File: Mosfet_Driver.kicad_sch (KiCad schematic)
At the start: 6 parts

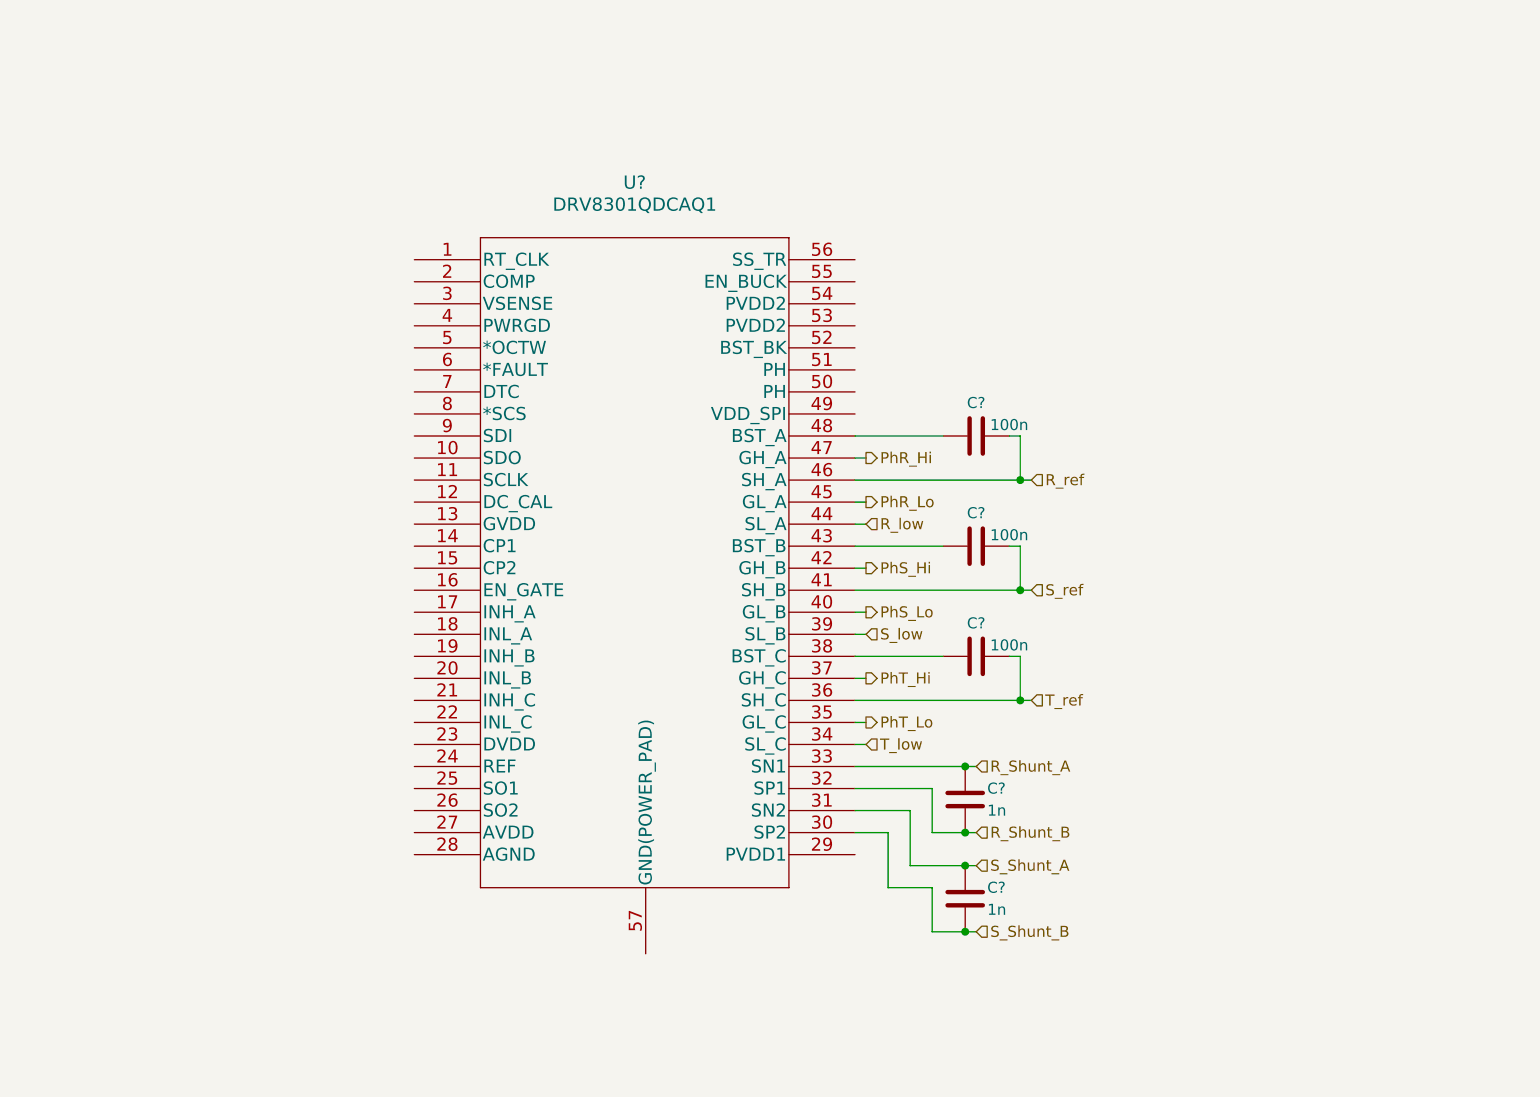
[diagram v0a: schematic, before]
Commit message: Finished basic schematic.
Need to add inline opamps and footprints to all components.
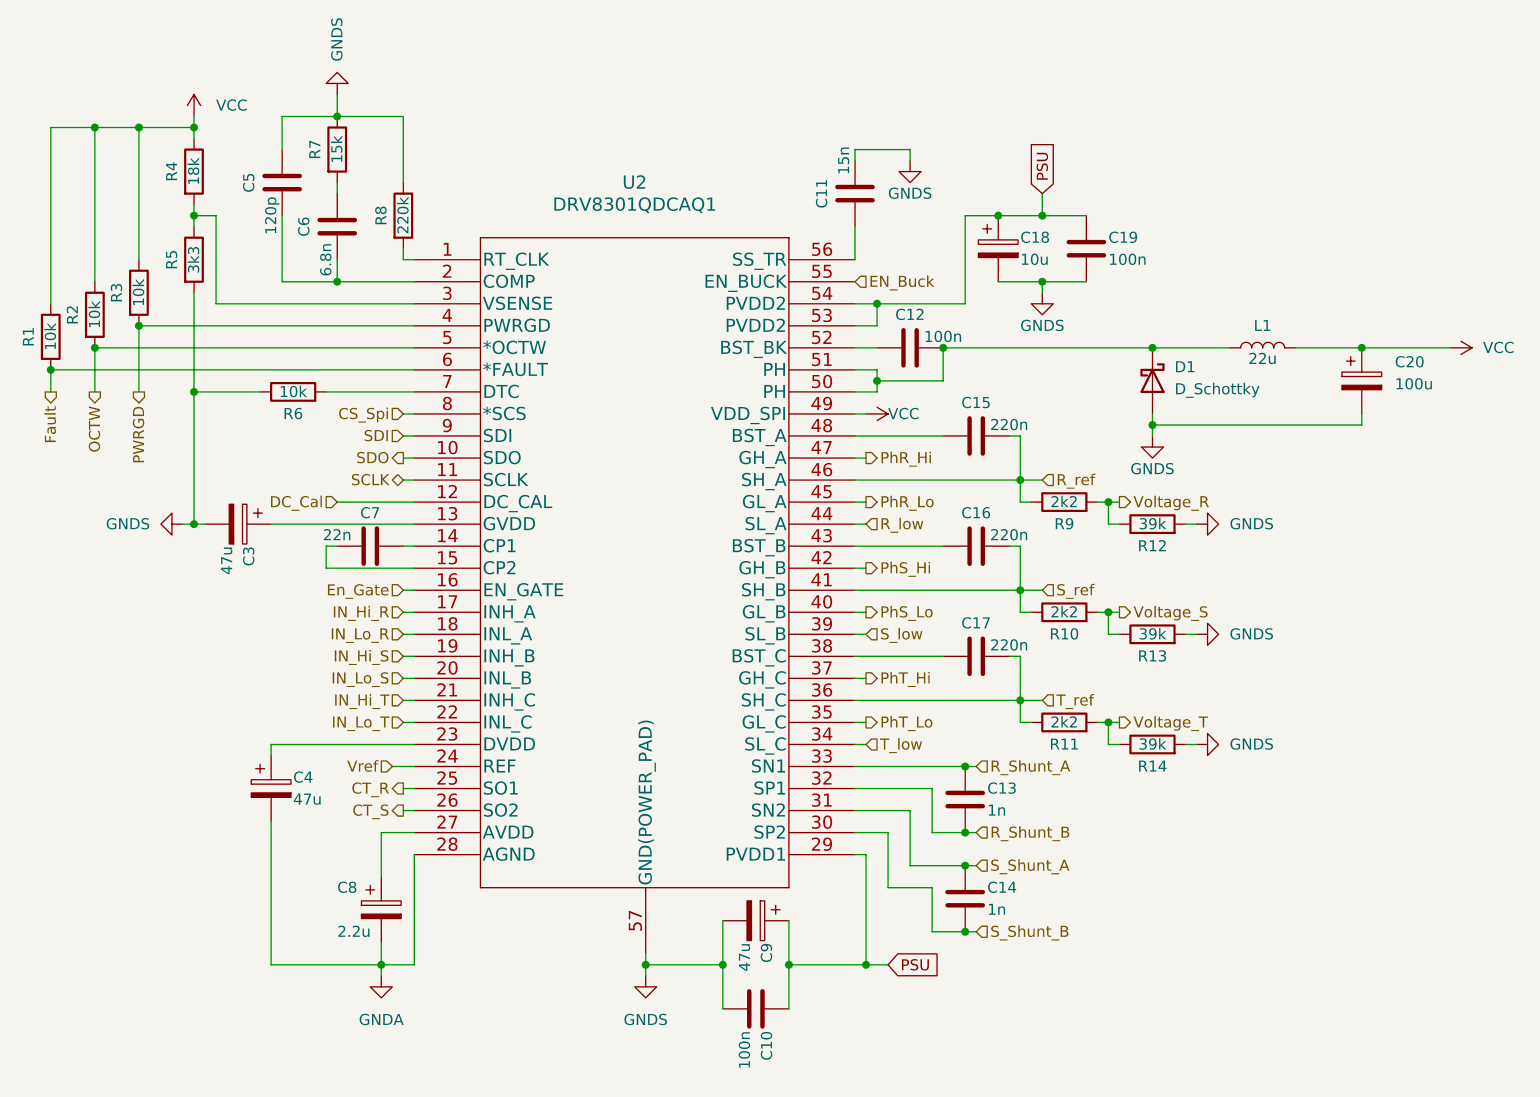
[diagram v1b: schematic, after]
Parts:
- added C10, C12, C19: 100n, symbol Device:C
- added C11: 15n, symbol Device:C
- added C18: 10u, symbol Device:C_Polarized
- added C20: 100u, symbol Device:C_Polarized
- added C3, C4, C9: 47u, symbol Device:C_Polarized
- added C5: 120p, symbol Device:C
- added C6: 6.8n, symbol Device:C
- added C7: 22n, symbol Device:C
- added C8: 2.2u, symbol Device:C_Polarized
- added D1: D_Schottky, symbol Device:D_Schottky
- added L1: 22u, symbol Device:L
- added R1, R2, R3, R6: 10k, Resistor_THT:R_Axial_DIN0207_L6.3mm_D2.5mm_P7.62mm_Horizontal, symbol Device:R
- added R10, R11, R9: 2k2, Resistor_THT:R_Axial_DIN0207_L6.3mm_D2.5mm_P7.62mm_Horizontal, symbol Device:R
- added R12, R13, R14: 39k, Resistor_THT:R_Axial_DIN0207_L6.3mm_D2.5mm_P7.62mm_Horizontal, symbol Device:R
- added R4: 18k, Resistor_THT:R_Axial_DIN0207_L6.3mm_D2.5mm_P7.62mm_Horizontal, symbol Device:R
- added R5: 3k3, Resistor_THT:R_Axial_DIN0207_L6.3mm_D2.5mm_P7.62mm_Horizontal, symbol Device:R
- added R7: 15k, Resistor_THT:R_Axial_DIN0207_L6.3mm_D2.5mm_P7.62mm_Horizontal, symbol Device:R
- added R8: 220k, Resistor_THT:R_Axial_DIN0207_L6.3mm_D2.5mm_P7.62mm_Horizontal, symbol Device:R
- C15, C16, C17: renamed from C?; value 100n -> 220n
- U2: renamed from U?; footprint DCA56_6P35X3P61_TEX -> drv8301qdcaq1:DRV8301QDCAQ1
- gave numbers to parts that had none: 2
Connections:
- net R_ref: now also R9.1
- net S_ref: now also R10.1
- net T_ref: now also R11.1
- net at U2.1 (RT_CLK): now also R8.2
- net SDO: now reaches U2.10 (SDO)
- net SCLK: now reaches U2.11 (SCLK)
- net DC_Cal: now reaches U2.12 (DC_CAL)
- net at U2.13 (GVDD): now also C3.1
- net at U2.14 (CP1): now also C7.1
- net at U2.15 (CP2): now also C7.2
- net En_Gate: now reaches U2.16 (EN_GATE)
- net IN_Hi_R: now reaches U2.17 (INH_A)
- net IN_Lo_R: now reaches U2.18 (INL_A)
- net IN_Hi_S: now reaches U2.19 (INH_B)
- net at U2.2 (COMP): now also C5.2, C6.2
- net IN_Lo_S: now reaches U2.20 (INL_B)
- net IN_Hi_T: now reaches U2.21 (INH_C)
- net IN_Lo_T: now reaches U2.22 (INL_C)
- net at U2.23 (DVDD): now also C4.1
- net Vref: now reaches U2.24 (REF)
- net CT_R: now reaches U2.25 (SO1)
- net CT_S: now reaches U2.26 (SO2)
- net at U2.27 (AVDD): now also C8.1
- net GNDA: now reaches U2.28 (AGND)
- net GNDA: now also C4.2, C8.2
- net PSU: now reaches U2.29 (PVDD1)
- net PSU: now also U2.53 (PVDD2), U2.54 (PVDD2), C10.1, C18.1, C19.1, C9.1
- net at U2.3 (VSENSE): now also R4.2, R5.1
- net PWRGD: now reaches U2.4 (PWRGD)
- net PWRGD: now also R3.2
- net VCC: now reaches U2.49 (VDD_SPI)
- net VCC: now also C20.1, L1.2, R1.1, R2.1, R3.1, R4.1
- net OCTW: now reaches U2.5 (*OCTW)
- net OCTW: now also R2.2
- net at U2.50 (PH): now also U2.51 (PH), C12.2, D1.1 (K), L1.1
- net at U2.52 (BST_BK): now also C12.1
- net EN_Buck: now reaches U2.55 (EN_BUCK)
- net at U2.56 (SS_TR): now also C11.1
- net GNDS: now reaches U2.57 (GND(POWER_PAD))
- net GNDS: now also C10.2, C11.2, C18.2, C19.2, C20.2, C3.2, C5.1, C9.2, D1.2 (A), R12.2, R13.2, R14.2, R5.2, R6.1, R7.1, R8.1
- net Fault: now reaches U2.6 (*FAULT)
- net Fault: now also R1.2
- net at U2.7 (DTC): now also R6.2
- net CS_Spi: now reaches U2.8 (*SCS)
- net SDI: now reaches U2.9 (SDI)
- new net: C6.1, R7.2
- new net Voltage_R: R12.1, R9.2
- new net Voltage_S: R10.2, R13.1
- new net Voltage_T: R11.2, R14.1
